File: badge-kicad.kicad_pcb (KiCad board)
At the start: 2 copper layers, 152.7 x 76.7 mm, 129 parts, among them J2 JTAG, P2 CONN_02X20, P3 FTDI BACKUP, P4 USB_MICRO_RIGHT, P5 LED OUT (DNP), SW1 RESET, SW2 POWERON, SW3 TM1000, SW4 UP, SW5 DN, SW6 LEFT, SW7 RIGHT, SW8 ENTER, U1 WS2812B, U10 WS2812B, U11 WS2812B, U12 WS2812B, U13 MKW01Z128, U14 FT232RL SSOP, U15 MF-REG-SOT235-3.3V-300mA, U16 MCP73831T-2ACI/OT, U18 LM386, U2 WS2812B, U3 WS2812B, U4 WS2812B, U5 WS2812B, U6 WS2812B, U7 WS2812B, U8 WS2812B, U9 WS2812B, Y1 EXS00A-CS02368

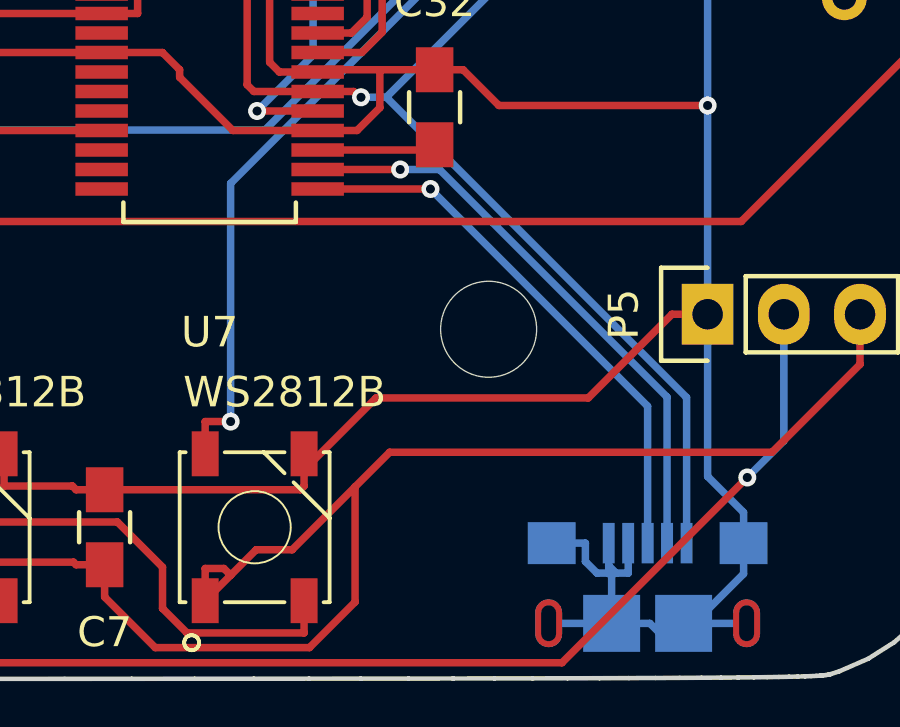
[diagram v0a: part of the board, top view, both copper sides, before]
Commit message: Move the P4-Net trace far, far away from H4. Potential issue if we resize the hole
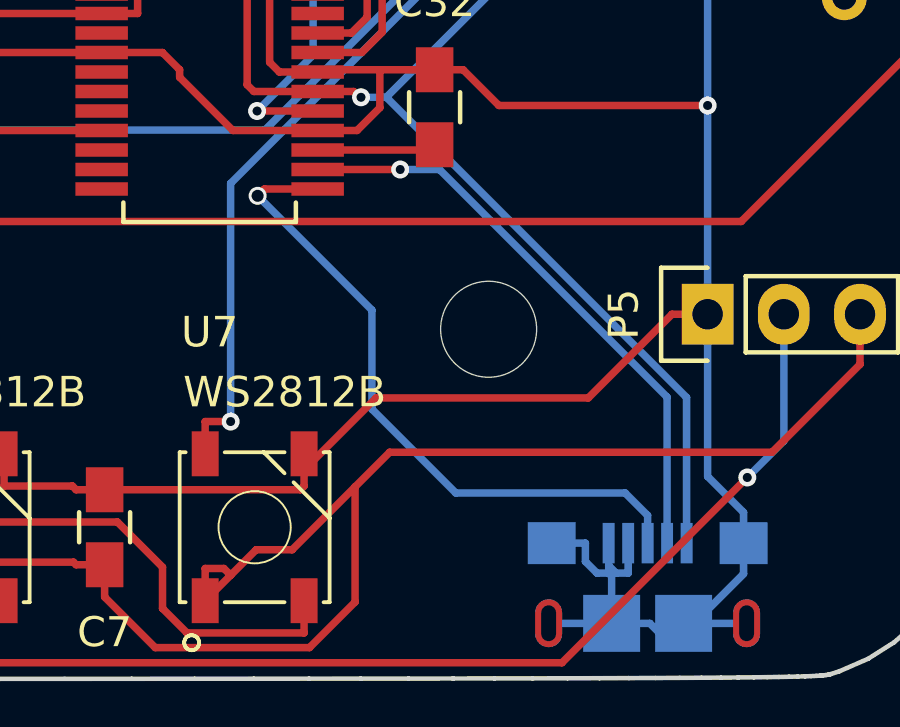
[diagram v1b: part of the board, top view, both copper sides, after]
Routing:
- net Net-(P4-Pad3): track 18.6 -> 22.4 mm
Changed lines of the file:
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@@
     (thickness 1.6)
     (drawings 370)
-    (tracks 1515)
+    (tracks 1520)
     (zones 0)
     (modules 129)
@@
     (38 B.Mask user)
     (39 F.Mask user)
-    (40 Dwgs.User user)
+    (40 Dwgs.User user hide)
     (41 Cmts.User user hide)
     (42 Eco1.User user hide)
@@
   (segment (start 187.7777 122.792) (end 187.7777 117.9228) (width 0.25) (layer B.Cu) (net 80) (status 10))
   (segment (start 176.13 110.337) (end 178.8827 110.337) (width 0.25) (layer F.Cu) (net 80) (status 10))
-  (via (at 179.8909 110.987) (size 0.6) (layers F.Cu B.Cu) (net 81))
-  (segment (start 187.13 118.2261) (end 179.8909 110.987) (width 0.25) (layer B.Cu) (net 81))
-  (segment (start 187.13 122.792) (end 187.13 118.2261) (width 0.25) (layer B.Cu) (net 81) (status 10))
-  (segment (start 176.13 110.987) (end 179.8909 110.987) (width 0.25) (layer F.Cu) (net 81) (status 10))
+  (segment (start 180.734 121.12) (end 186.38237 121.12) (width 0.25) (layer B.Cu) (net 81))
+  (segment (start 186.38237 121.12) (end 187.13 121.86763) (width 0.25) (layer B.Cu) (net 81))
+  (segment (start 187.13 121.86763) (end 187.13 122.792) (width 0.25) (layer B.Cu) (net 81))
+  (segment (start 177.94 118.326) (end 180.734 121.12) (width 0.25) (layer B.Cu) (net 81))
+  (segment (start 177.94 115.024) (end 177.94 118.326) (width 0.25) (layer B.Cu) (net 81))
+  (segment (start 174.13 111.214) (end 177.94 115.024) (width 0.25) (layer B.Cu) (net 81))
+  (segment (start 176.13 110.987) (end 174.357 110.987) (width 0.25) (layer F.Cu) (net 81))
+  (segment (start 174.357 110.987) (end 174.13 111.214) (width 0.25) (layer F.Cu) (net 81))
+  (via (at 174.13 111.214) (size 0.6) (drill 0.4) (layers F.Cu B.Cu) (net 81))
   (via (at 149.58 91.872) (size 0.6) (layers F.Cu B.Cu) (net 82))
   (segment (start 150.06 91.632) (end 151.955 91.637) (width 0.25) (layer B.Cu) (net 82))

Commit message: update for fabrication rev3
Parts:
- added ?: , logos:hw_200dpi, B.Cu at (166.6, 69.5)
- added ?: , logos:grimm_600dpi, B.Cu at (167.5, 106.2)
- added ?: , logos:redteam_31_40, B.Cu at (167.3, 83.3)
- added TP11: PTC1, Measurement_Points:Measurement_Point_Round-TH_Small, F.Cu at (109.9, 89.4)
- added TP12: PTB0, Measurement_Points:Measurement_Point_Round-TH_Small, F.Cu at (132.5, 96.7)
- added TP13: PTE16, Measurement_Points:Measurement_Point_Round-TH_Small, F.Cu at (133.9, 83.4)
- added TP14: PTB1, Measurement_Points:Measurement_Point_Round-TH_Small, F.Cu at (168.0, 97.0)
- added TP6: PTA19, Measurement_Points:Measurement_Point_Round-TH_Small, F.Cu at (125.4, 92.9)
- added TP7: PTC2, Measurement_Points:Measurement_Point_Round-TH_Small, F.Cu at (109.9, 99.3)
- added TP8: PTC4, Measurement_Points:Measurement_Point_Round-TH_Small, F.Cu at (109.9, 96.5)
- BT1: value Battery 3.7v 1000mAh -> Battery 3.7v 1200mAh
- U13: footprint jna-parts:98ASA00302D -> jna-parts:mkw01z128
- moved C42 41.8 mm to (162.2, 76.4), turned to 0 degrees
- moved TP9 34.4 mm to (196.7, 70.3)
- moved TP2 30.3 mm to (198.8, 70.3)
- moved TP1 28.1 mm to (200.8, 70.3)
- moved C36 4.59 mm to (140.0, 80.5), turned to 0 degrees
- moved C34 1.55 mm to (140.0, 83.7), turned to 180 degrees
- moved U13 0.12 mm to (148.8, 89.2)
- turned C33 to 90 degrees
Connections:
- BT1 pad 1: VBAT -> VCHG
- C15 pad 1: VBAT -> VCHG
- SW2 pad 1: Net-(SW2-Pad1) -> VCHG
- SW2 pad 2: VCC -> VBAT
- U13 pad 61: GND -> (no net)
- U13 pad 62: GND -> (no net)
- U15 pad 5: Net-(SW2-Pad1) -> VCC
- U16 pad 3: VBAT -> VCHG
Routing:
- net VCHG: track 0.00 -> 115.1 mm, vias 0 -> 1
- net GND: track 835.8 -> 762.3 mm, vias 4 -> 6
- net PTE16: track 48.5 -> 119.6 mm, vias 2 -> 1
- net VBAT: track 313.8 -> 365.7 mm, vias 6 -> 5
- net SWENTER: track 104.3 -> 153.7 mm
- net Net-(C42-Pad2): track 53.3 -> 5.07 mm
- net DACOUT: track 31.1 -> 60.1 mm, vias 2 -> 4
- net Net-(SW2-Pad1): track 28.9 -> 0.00 mm, vias 1 -> 0
- net Net-(C42-Pad1): track 61.0 -> 34.7 mm, vias 2 -> 0
- net DIO0: track 46.2 -> 29.4 mm
- net VCC: track 306.0 -> 321.3 mm, vias 7 -> 9
- net UART_TX: track 64.6 -> 49.7 mm, vias 2 -> 4
- net PTB1: track 61.0 -> 46.2 mm, vias 4 -> 3
- net UART0_CTS: track 40.7 -> 54.8 mm
- net PTB0: track 118.5 -> 130.9 mm, vias 3 -> 5
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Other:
- board text added: "+VBAT"
- board text added: "PTA19"
- board text added: "PTB0"
- board text added: "PTB1"
- board text added: "PTC1"
- board text added: "PTC2"
- board text added: "PTC4"
- board text added: "PTE16"
- board text added: "Thanks to our sponsors and all of our kickstarter backers!"
- board text added: "The Ides of DEFCON - Revision 2 - SPQR DEFCON 25 (2017) - Limited Edition John Adams @netik (PCB, HW, SW) Bill Paul (Drivers, Board bringup, HW, SW) Egan Hirvela (Game Mechanics) Matthew Harris (Art, Character Design) Based on ChibiOS RTOS (http://chibios.org) HAIL CAESAR! Designed in San Francisco, California Fabricated in Houston, Texas at Macrofab https://retina.net/spqr"
- board text removed: "PWR OK"
- board text removed: "SPQR - The Ides of March - Revision 2 DEFCON 25 (2017) John Adams @netik (PCB, HW, SW) Bill Paul (Drivers, Board bringup, HW, SW) Egan Hirvela (Game Mechanics) Matthew Harris (Art, Character Design) Based on ChibiOS RTOS (http://chibios.org) HAIL CASEAR! Made in San Francisco https://retina.net/spqr"

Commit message: check in changes before modifiying footprint for rev4
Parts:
- added G***: LOGO, logos:avast_36_11, B.Cu at (161.6, 62.0)
- P4: value USB_MICRO_RIGHT -> CHARGE/CONSOLE
- moved ? 49.2 mm to (132.9, 118.4)
- moved ? 15.0 mm to (166.2, 121.1)
- moved C43 11.1 mm to (166.2, 77.2), turned to 270 degrees
- moved R19 6.40 mm to (163.2, 81.7), turned to 270 degrees
- moved ? 4.93 mm to (164.8, 74.1)
- moved C47 4.09 mm to (170.3, 85.2), turned to 270 degrees
- moved C36 3.22 mm to (143.2, 80.8), turned to 180 degrees
- moved C25 2.55 mm to (125.4, 66.8)
- moved C34 1.24 mm to (139.8, 84.9), turned to 90 degrees
- moved C42 1.21 mm to (163.2, 77.2), turned to 270 degrees
- moved R20 0.73 mm to (166.3, 81.7), turned to 270 degrees
- moved R22 0.60 mm to (166.2, 72.7), turned to 90 degrees
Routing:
- net GND: track 762.3 -> 715.1 mm
- net Net-(C42-Pad1): track 34.7 -> 15.4 mm
- net Net-(C43-Pad2): track 21.0 -> 2.27 mm
- net Net-(C26-Pad1): track 46.1 -> 31.7 mm
- net PWM_SOUND: track 32.7 -> 23.8 mm
- net VCC: track 321.3 -> 328.6 mm, vias 9 -> 8
- net PTB0: track 130.9 -> 136.6 mm
- net Net-(C47-Pad1): track 42.9 -> 37.6 mm
- net Net-(C42-Pad2): track 5.07 -> 2.36 mm
- net Net-(C47-Pad2): track 9.01 -> 6.62 mm
- net Net-(C25-Pad1): track 8.79 -> 6.76 mm
- net CLOCKOUT: track 43.2 -> 41.5 mm
- net DACOUT: track 60.1 -> 58.7 mm
- net UART_RX: track 54.5 -> 55.7 mm
- net Net-(C44-Pad1): track 29.2 -> 30.2 mm
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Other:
- board text added: "CHARGED"
- board text added: "POWER"
- board text added: "The Ides of DEFCON - Revision 3 - SPQR DEFCON 25 (2017) - Limited Edition John Adams @netik (PCB, HW, SW) Bill Paul (Drivers, Board bringup, HW, SW) Egan Hirvela (Game Mechanics) Matthew Harris (Art, Character Design) Based on ChibiOS RTOS (http://chibios.org) HAIL CAESAR! Designed in San Francisco, California Fabricated in Houston, Texas at Macrofab https://dc25spqr.com"
- board text added: "VBATT (+)"
- board text removed: "CHG DONE"
- board text removed: "The Ides of DEFCON - Revision 2 - SPQR DEFCON 25 (2017) - Limited Edition John Adams @netik (PCB, HW, SW) Bill Paul (Drivers, Board bringup, HW, SW) Egan Hirvela (Game Mechanics) Matthew Harris (Art, Character Design) Based on ChibiOS RTOS (http://chibios.org) HAIL CAESAR! Designed in San Francisco, California Fabricated in Houston, Texas at Macrofab https://retina.net/spqr"

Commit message: update for rev4
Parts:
- added ?: , logos:phobos_19mm_x_5.5mm, B.Cu at (133.2, 74.4)
- added G***: LOGO, logos:urbane_val, B.Cu at (117.7, 84.3)
- U13: footprint jna-parts:mkw01z128 -> jna-parts:mkw01z128-updated
- moved TP13 6.91 mm to (128.0, 79.8)
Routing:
- net GND: track 715.1 -> 703.6 mm
- net PTE16: track 119.6 -> 127.4 mm
- net SWENTER: track 153.7 -> 154.2 mm
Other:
- board text added: "uggcf://qp25fcde.pbz/vgortvaf"

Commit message: final commit for production
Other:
- board text added: "ON"
- board text added: "The Ides of DEF CON - Revision 5 DEF CON 25 (2017) - Limited Edition of 225 John Adams @netik (PCB, HW, SW) Bill Paul (Drivers, Board bringup, HW, SW) Egan Hirvela (Game Mechanics) Matthew Harris (Art, Character Design) Based on ChibiOS RTOS (http://chibios.org) HAIL CAESAR! Designed in San Francisco, California Fabricated in Houston, Texas at Macrofab https://dc25spqr.com"
- board text removed: "The Ides of DEFCON - Revision 3 - SPQR DEFCON 25 (2017) - Limited Edition John Adams @netik (PCB, HW, SW) Bill Paul (Drivers, Board bringup, HW, SW) Egan Hirvela (Game Mechanics) Matthew Harris (Art, Character Design) Based on ChibiOS RTOS (http://chibios.org) HAIL CAESAR! Designed in San Francisco, California Fabricated in Houston, Texas at Macrofab https://dc25spqr.com"
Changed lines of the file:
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@@
     (area 72.606224 50.56983 225.427963 127.397751)
     (thickness 1.6)
-    (drawings 382)
+    (drawings 383)
     (tracks 1542)
     (zones 0)
@@
     (34 B.Paste user)
     (35 F.Paste user)
-    (36 B.SilkS user hide)
+    (36 B.SilkS user)
     (37 F.SilkS user)
     (38 B.Mask user)
@@
       (drillshape 0)
       (scaleselection 1)
-      (outputdirectory fabrication-rev4/))
+      (outputdirectory fabrication-final))
   )
   (net 0 "")
@@
     (descr "Ultraminiature Surface Mount Slide Switch")
     (attr smd)
-    (fp_text reference SW2 (at -1.5 3.175 180) (layer B.SilkS)
+    (fp_text reference SW2 (at -1.5 3.175 180) (layer B.SilkS) hide
       (effects (font (size 1 1) (thickness 0.15)) (justify mirror))
     )
@@
       (net 100 "Net-(U11-PadP$2)"))
   )
+  (gr_text ON (at 111.03 119.762) (layer B.SilkS)
+    (effects (font (size 1.5 1.5) (thickness 0.3)) (justify mirror))
+  )
   (gr_text uggcf://qp25fcde.pbz/vgortvaf (at 110.53 74.262 90) (layer F.SilkS)
     (effects (font (size 1 1) (thickness 0.25)))
@@
     (effects (font (size 1 1) (thickness 0.2)))
   )
-  (gr_text "The Ides of DEFCON - Revision 3 - SPQR\nDEFCON 25 (2017) - Limited Edition\n\nJohn Adams @netik (PCB, HW, SW)\nBill Paul (Drivers, Board bringup, HW, SW)\nEgan Hirvela (Game Mechanics)\nMatthew Harris (Art, Character Design)\n\nBased on ChibiOS RTOS (http://chibios.org)\n\n\n\n\nHAIL CAESAR!\n\nDesigned in San Francisco, California\nFabricated in Houston, Texas at Macrofab\nhttps://dc25spqr.com" (at 215.532 93.942) (layer B.SilkS)
+  (gr_text "The Ides of DEF CON - Revision 5\nDEF CON 25 (2017) - Limited Edition of 225\n\nJohn Adams @netik (PCB, HW, SW)\nBill Paul (Drivers, Board bringup, HW, SW)\nEgan Hirvela (Game Mechanics)\nMatthew Harris (Art, Character Design)\n\nBased on ChibiOS RTOS (http://chibios.org)\n\n\n\n\nHAIL CAESAR!\n\nDesigned in San Francisco, California\nFabricated in Houston, Texas at Macrofab\nhttps://dc25spqr.com" (at 215.532 93.942) (layer B.SilkS)
     (effects (font (size 1 1) (thickness 0.2)) (justify left mirror))
   )
@@
     (effects (font (size 1 1) (thickness 0.127)))
   )
-  (gr_text CTS (at 142.53 107.762) (layer F.SilkS)
+  (gr_text CTS (at 142.53 112.762) (layer F.SilkS)
     (effects (font (size 1 1) (thickness 0.2)) (justify left))
   )
@@
     (effects (font (size 1.5 1.5) (thickness 0.3)) (justify mirror))
   )
-  (gr_text FTDI (at 144.92 105.372) (layer F.SilkS)
+  (gr_text FTDI (at 145.03 114.762) (layer F.SilkS)
     (effects (font (size 1.5 1.5) (thickness 0.3)))
   )
